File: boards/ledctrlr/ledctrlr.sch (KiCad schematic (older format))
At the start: 55 parts, among them IC1 ATMEGA168-P, IC2 SN75176B, J1 RJ45, J2 RJ45, SW1 SW_PUSH, U1 LM7805, X1 CRYSTAL

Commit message: rev 2.0 routed
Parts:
- LED0, LED2, LED3, LED4: DigikeyPart (none) -> ED2563-ND; Part (none) -> OSTTA040161
- LED1: Digikey (none) -> ED2563-ND; Part (none) -> OSTTA040161
- TLC1, TLC2, TLC3: footprint (none) -> DIP-28__300; DigikeyPart (none) -> 296-17732-5-ND; Part (none) -> TLC5940NT
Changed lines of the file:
@@
-EESchema Schematic File Version 2  date Mon 29 Oct 2012 07:47:27 PM EDT
+EESchema Schematic File Version 2  date Sat 03 Nov 2012 11:20:31 PM EDT
 LIBS:power
 LIBS:device
@@
 Sheet 1 1
 Title "5-RGB LED Controller Board"
-Date "29 oct 2012"
+Date "4 nov 2012"
 Rev "2.0"
 Comp "J. Colosimo"
@@
 F 1 "CONN_4" V 10300 2950 50  0000 C CNN
 F 2 "OSTTA040161" V 10400 2950 50  0001 C CNN
+F 4 "OSTTA040161" H 10250 2950 60  0001 C CNN "Part"
+F 5 "ED2563-ND" V 10250 2950 60  0001 C CNN "DigikeyPart"
 	1    10250 2950
 	1    0    0    -1
@@
 F 1 "CONN_4" V 10300 3450 50  0000 C CNN
 F 2 "OSTTA040161" V 10400 3450 50  0001 C CNN
+F 4 "OSTTA040161" H 10250 3450 60  0001 C CNN "Part"
+F 5 "ED2563-ND" V 10250 3450 60  0001 C CNN "Digikey"
 	1    10250 3450
 	1    0    0    -1
@@
 F 1 "CONN_4" V 10300 3950 50  0000 C CNN
 F 2 "OSTTA040161" V 10400 3950 50  0001 C CNN
+F 4 "OSTTA040161" H 10250 3950 60  0001 C CNN "Part"
+F 5 "ED2563-ND" V 10250 3950 60  0001 C CNN "DigikeyPart"
 	1    10250 3950
 	1    0    0    -1
@@
 F 1 "CONN_4" V 10300 4450 50  0000 C CNN
 F 2 "OSTTA040161" V 10400 4450 50  0001 C CNN
+F 4 "OSTTA040161" H 10250 4450 60  0001 C CNN "Part"
+F 5 "ED2563-ND" V 10250 4450 60  0001 C CNN "DigikeyPart"
 	1    10250 4450
 	1    0    0    -1
@@
 F 1 "CONN_4" V 10300 4950 50  0000 C CNN
 F 2 "OSTTA040161" V 10400 4950 50  0001 C CNN
+F 4 "OSTTA040161" H 10250 4950 60  0001 C CNN "Part"
+F 5 "ED2563-ND" V 10250 4950 60  0001 C CNN "DigikeyPart"
 	1    10250 4950
 	1    0    0    -1
@@
 F 0 "TLC1" H 7800 2300 60  0000 C CNN
 F 1 "TLC5940" H 7850 1750 60  0000 C CNN
+F 2 "DIP-28__300" H 7850 1850 60  0001 C CNN
+F 4 "TLC5940NT" H 7800 1550 60  0001 C CNN "Part"
+F 5 "296-17732-5-ND" H 7800 1550 60  0001 C CNN "DigikeyPart"
 	1    7800 1550
 	-1   0    0    -1
@@
 F 0 "TLC2" H 7800 4450 60  0000 C CNN
 F 1 "TLC5940" H 7850 3900 60  0000 C CNN
+F 2 "DIP-28__300" H 7850 4000 60  0001 C CNN
+F 4 "TLC5940NT" H 7800 3700 60  0001 C CNN "Part"
+F 5 "296-17732-5-ND" H 7800 3700 60  0001 C CNN "DigikeyPart"
 	1    7800 3700
 	-1   0    0    -1
@@
 F 0 "TLC3" H 7800 6600 60  0000 C CNN
 F 1 "TLC5940" H 7850 6050 60  0000 C CNN
+F 2 "DIP-28__300" H 7850 6150 60  0001 C CNN
+F 4 "TLC5940NT" H 7800 5850 60  0001 C CNN "Part"
+F 5 "296-17732-5-ND" H 7800 5850 60  0001 C CNN "DigikeyPart"
 	1    7800 5850
 	-1   0    0    -1

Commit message: clean up routing, switch GSCLK to PB0
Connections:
- net GSCLK: now also IC1.14 ((PCINT0/CLKO/ICP1)PB0); no longer IC1.5 ((PCINT19/OC2B/INT1)PD3)
- net XPB0 renamed XPD3
- net XPD3: now also IC1.5 ((PCINT19/OC2B/INT1)PD3); no longer IC1.14 ((PCINT0/CLKO/ICP1)PB0)
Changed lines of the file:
@@
-EESchema Schematic File Version 2  date Sat 03 Nov 2012 11:20:31 PM EDT
+EESchema Schematic File Version 2  date Mon 05 Nov 2012 06:34:16 PM EST
 LIBS:power
 LIBS:device
@@
 Sheet 1 1
 Title "5-RGB LED Controller Board"
-Date "4 nov 2012"
+Date "5 nov 2012"
 Rev "2.0"
 Comp "J. Colosimo"
@@
 F 5 "N/A" H 4700 4500 60  0001 C CNN "DigikeyPart"
 	1    4700 4500
-	1    0    0    -1
-$EndComp
-$Comp
-L CONN_1 PX2
-U 1 1 4DDC2882
-P 4700 2500
-F 0 "PX2" H 4750 2500 40  0000 L CNN
-F 1 "CONN_1" H 4700 2555 30  0001 C CNN
-F 2 "PAD" H 4790 2460 60  0001 C CNN
-F 4 "N/A" H 4700 2500 60  0001 C CNN "Part"
-F 5 "N/A" H 4700 2500 60  0001 C CNN "DigikeyPart"
-	1    4700 2500
 	1    0    0    -1
 $EndComp
@@
 Text Label 5300 2700 0    60   ~ 0
 BLANK
-Text Label 5350 4400 0    60   ~ 0
+Text Label 5300 2500 0    60   ~ 0
 GSCLK
 Text Label 4600 4600 0    60   ~ 0
@@
 Text Label 4700 2100 0    60   ~ 0
 XTAL2
-Text Label 4500 2500 0    60   ~ 0
-XPB0
 Text Label 4500 2900 0    60   ~ 0
 XPB4
@@
 	-1   0    0    1
 $EndComp
+$Comp
+L CONN_1 PX2
+U 1 1 50984858
+P 4700 4400
+F 0 "PX2" H 4750 4400 40  0000 L CNN
+F 1 "CONN_1" H 4700 4455 30  0001 C CNN
+F 2 "PAD" H 4790 4360 60  0001 C CNN
+F 4 "N/A" H 4700 4400 60  0001 C CNN "Part"
+F 5 "N/A" H 4700 4400 60  0001 C CNN "DigikeyPart"
+	1    4700 4400
+	1    0    0    -1
+$EndComp
+Text Label 4500 4400 0    60   ~ 0
+XPD3
 Wire Wire Line
 	1700 1550 1700 1850
@@
 Wire Wire Line
 	6400 2600 4500 2600
-Connection ~ 6650 4400
-Wire Wire Line
-	4500 4400 6650 4400
 Wire Wire Line
 	6150 950  7200 950
@@
 	4500 3850 4550 3850
 Wire Wire Line
-	4500 2500 4550 2500
-Wire Wire Line
 	2100 6300 2250 6300
 Connection ~ 2100 6300
@@
 Wire Wire Line
 	8000 5450 8000 5450
+Wire Wire Line
+	4500 4400 4550 4400
+Wire Wire Line
+	4500 2500 6650 2500
+Connection ~ 6650 2500
 $EndSCHEMATC

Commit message: clean up routing, return GSCLK to PD3, initial gerber export
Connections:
- net GSCLK: now also IC1.5 ((PCINT19/OC2B/INT1)PD3); no longer IC1.14 ((PCINT0/CLKO/ICP1)PB0)
- net XPD3 renamed XPB0
- net XPB0: now also IC1.14 ((PCINT0/CLKO/ICP1)PB0); no longer IC1.5 ((PCINT19/OC2B/INT1)PD3)
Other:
- moved on the sheet: PX2
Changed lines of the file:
@@
-EESchema Schematic File Version 2  date Mon 05 Nov 2012 06:34:16 PM EST
+EESchema Schematic File Version 2  date Wed 07 Nov 2012 06:37:59 AM EST
 LIBS:power
 LIBS:device
@@
 Sheet 1 1
 Title "5-RGB LED Controller Board"
-Date "5 nov 2012"
+Date "7 nov 2012"
 Rev "2.0"
 Comp "J. Colosimo"
@@
 Text Label 5300 2700 0    60   ~ 0
 BLANK
-Text Label 5300 2500 0    60   ~ 0
+Text Label 5300 4400 0    60   ~ 0
 GSCLK
 Text Label 4600 4600 0    60   ~ 0
@@
 L CONN_1 PX2
 U 1 1 50984858
-P 4700 4400
-F 0 "PX2" H 4750 4400 40  0000 L CNN
-F 1 "CONN_1" H 4700 4455 30  0001 C CNN
-F 2 "PAD" H 4790 4360 60  0001 C CNN
-F 4 "N/A" H 4700 4400 60  0001 C CNN "Part"
-F 5 "N/A" H 4700 4400 60  0001 C CNN "DigikeyPart"
-	1    4700 4400
-	1    0    0    -1
-$EndComp
-Text Label 4500 4400 0    60   ~ 0
-XPD3
+P 4700 2500
+F 0 "PX2" H 4750 2500 40  0000 L CNN
+F 1 "CONN_1" H 4700 2555 30  0001 C CNN
+F 2 "PAD" H 4790 2460 60  0001 C CNN
+F 4 "N/A" H 4700 2500 60  0001 C CNN "Part"
+F 5 "N/A" H 4700 2500 60  0001 C CNN "DigikeyPart"
+	1    4700 2500
+	1    0    0    -1
+$EndComp
+Text Label 4500 2500 0    60   ~ 0
+XPB0
 Wire Wire Line
 	1700 1550 1700 1850
@@
 	8000 5450 8000 5450
 Wire Wire Line
-	4500 4400 4550 4400
-Wire Wire Line
-	4500 2500 6650 2500
-Connection ~ 6650 2500
+	4500 4400 6650 4400
+Connection ~ 6650 4400
+Wire Wire Line
+	4500 2500 4550 2500
 $EndSCHEMATC

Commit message: clean up ground routing, get rid of npth
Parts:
- LED0, LED1, LED2, LED3, LED4: footprint OSTTA040161 -> OSTTA040161p
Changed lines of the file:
@@
-EESchema Schematic File Version 2  date Wed 07 Nov 2012 06:37:59 AM EST
+EESchema Schematic File Version 2  date Wed 14 Nov 2012 04:07:55 PM EST
 LIBS:power
 LIBS:device
@@
 F 0 "LED0" V 10200 2950 50  0000 C CNN
 F 1 "CONN_4" V 10300 2950 50  0000 C CNN
-F 2 "OSTTA040161" V 10400 2950 50  0001 C CNN
+F 2 "OSTTA040161p" V 10400 2950 50  0001 C CNN
 F 4 "OSTTA040161" H 10250 2950 60  0001 C CNN "Part"
 F 5 "ED2563-ND" V 10250 2950 60  0001 C CNN "DigikeyPart"
@@
 F 0 "LED1" V 10200 3450 50  0000 C CNN
 F 1 "CONN_4" V 10300 3450 50  0000 C CNN
-F 2 "OSTTA040161" V 10400 3450 50  0001 C CNN
+F 2 "OSTTA040161p" V 10400 3450 50  0001 C CNN
 F 4 "OSTTA040161" H 10250 3450 60  0001 C CNN "Part"
 F 5 "ED2563-ND" V 10250 3450 60  0001 C CNN "Digikey"
@@
 F 0 "LED2" V 10200 3950 50  0000 C CNN
 F 1 "CONN_4" V 10300 3950 50  0000 C CNN
-F 2 "OSTTA040161" V 10400 3950 50  0001 C CNN
+F 2 "OSTTA040161p" V 10400 3950 50  0001 C CNN
 F 4 "OSTTA040161" H 10250 3950 60  0001 C CNN "Part"
 F 5 "ED2563-ND" V 10250 3950 60  0001 C CNN "DigikeyPart"
@@
 F 0 "LED3" V 10200 4450 50  0000 C CNN
 F 1 "CONN_4" V 10300 4450 50  0000 C CNN
-F 2 "OSTTA040161" V 10400 4450 50  0001 C CNN
+F 2 "OSTTA040161p" V 10400 4450 50  0001 C CNN
 F 4 "OSTTA040161" H 10250 4450 60  0001 C CNN "Part"
 F 5 "ED2563-ND" V 10250 4450 60  0001 C CNN "DigikeyPart"
@@
 F 0 "LED4" V 10200 4950 50  0000 C CNN
 F 1 "CONN_4" V 10300 4950 50  0000 C CNN
-F 2 "OSTTA040161" V 10400 4950 50  0001 C CNN
+F 2 "OSTTA040161p" V 10400 4950 50  0001 C CNN
 F 4 "OSTTA040161" H 10250 4950 60  0001 C CNN "Part"
 F 5 "ED2563-ND" V 10250 4950 60  0001 C CNN "DigikeyPart"

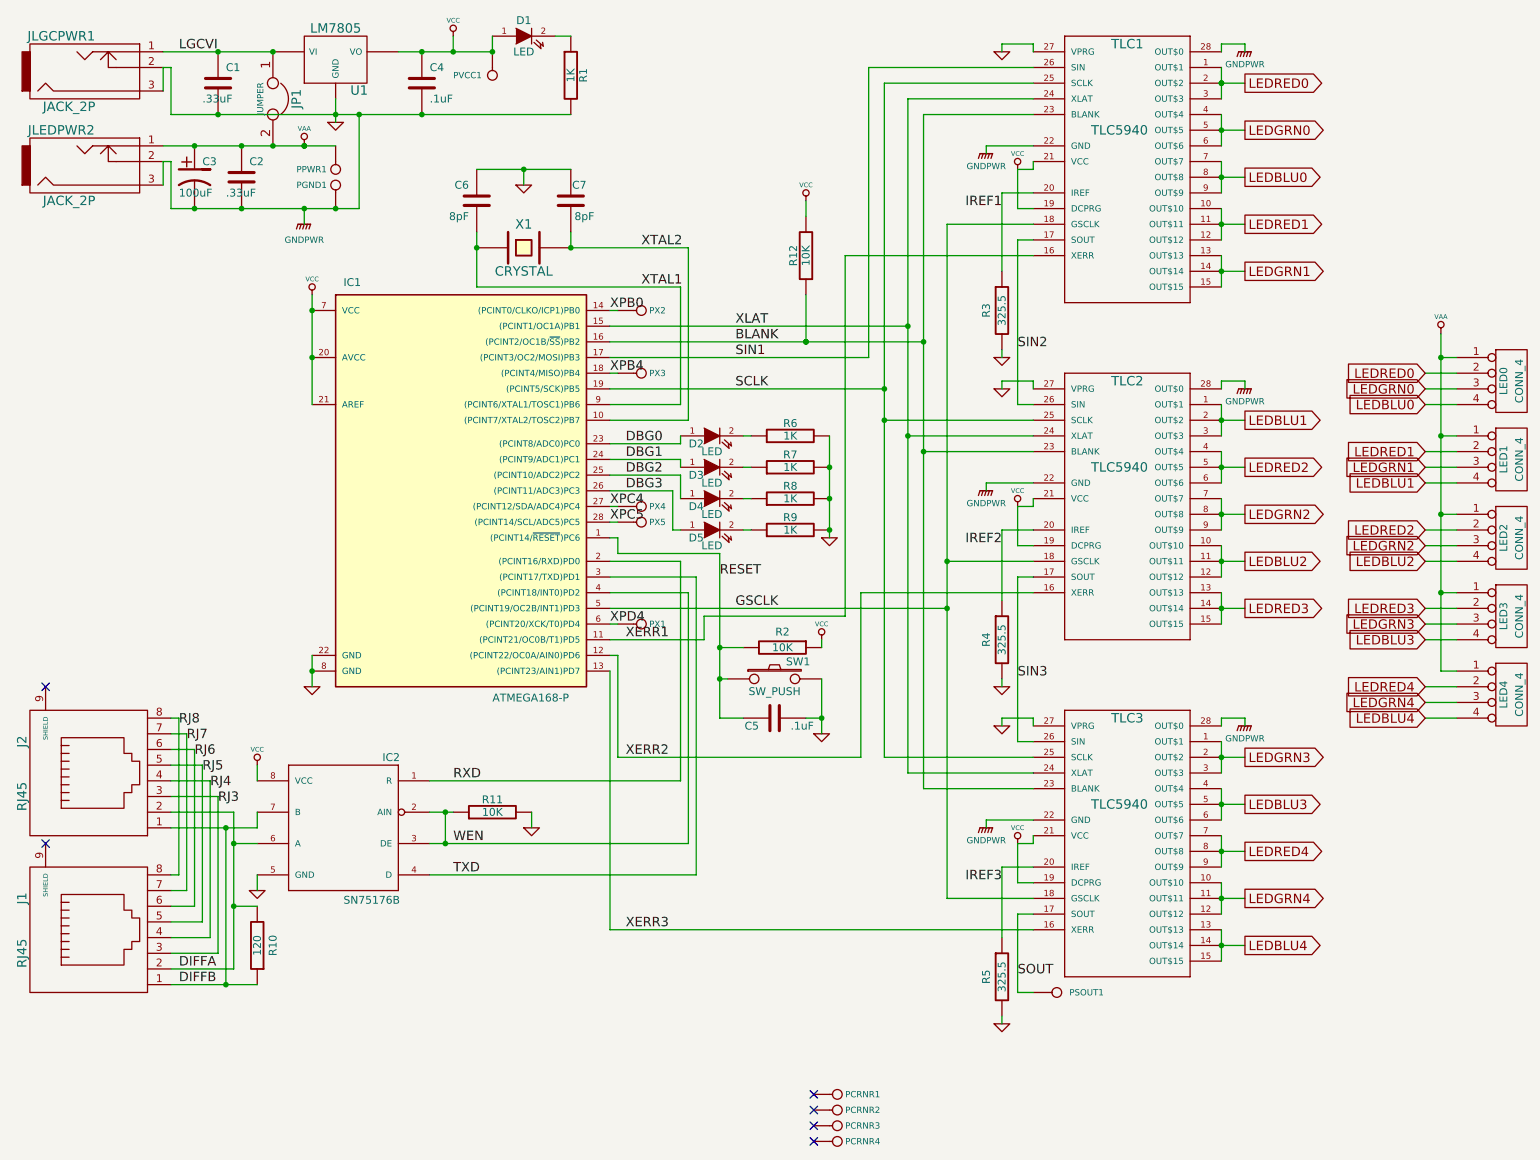
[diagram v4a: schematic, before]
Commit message: add schematics and footprints for green and black NRF24L01+ modules
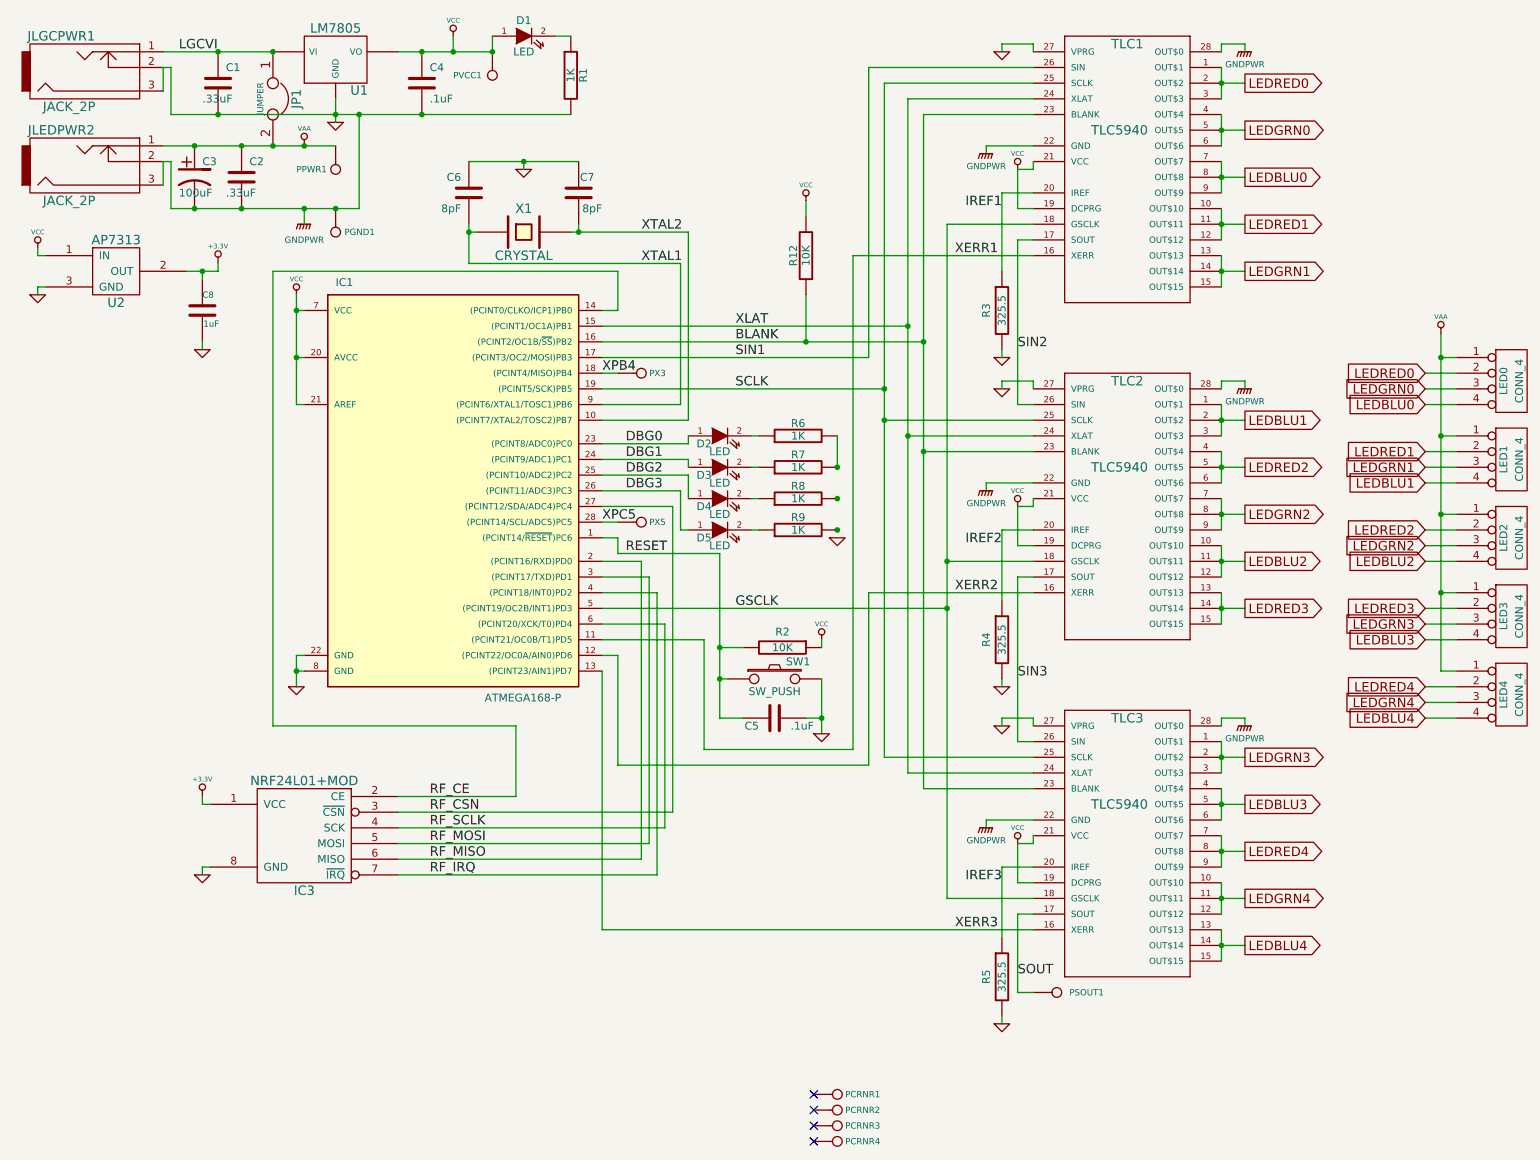
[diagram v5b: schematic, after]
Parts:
- removed IC2: SN75176B, SOIC8, symbol SN75176B
- removed J1, J2: RJ45, RJ45_8, symbol RJ45
- removed PX1, PX2, PX4: CONN_1, PAD, symbol CONN_1
- removed R10: 120, SM0805, symbol R
- removed R11: 10K, SM0805, symbol R
- added C8: 1uF, SM0805, symbol C
- added IC3: NRF24L01+MOD, NRF24LO1+MOD_GRN, symbol NRF24L01+MOD
- added U2: AP7313, SOT23, symbol AP7313
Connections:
- net GND: now also C8.2, IC3.8 (GND), U2.3 (GND); no longer R6.2, R7.2, R8.2, R9.2
- net VCC: now also U2.1 (IN)
- net RXD renamed RF_MISO
- net RF_MISO: now also IC3.6 (MISO)
- net TXD renamed RF_MOSI
- net RF_MOSI: now also IC3.5 (MOSI)
- net WEN renamed RF_IRQ
- net RF_IRQ: now also IC3.7 (~IRQ)
- net XPB0 renamed RF_CE
- net RF_CE: now also IC3.2 (CE)
- net XPC4 renamed RF_CSN
- net RF_CSN: now also IC3.3 (~CSN)
- net XPD4 renamed RF_SCLK
- net RF_SCLK: now also IC3.4 (SCK)
- new net: R6.2, R7.2
- new net +3.3V: C8.1, IC3.1 (VCC), U2.2 (OUT)
- no-connect marks 6 -> 4
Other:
- moved on the sheet: C6, C7, D2, D3, D4, D5, IC1, PGND1, R6, R7, R8, R9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

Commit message: transmit appears to be working
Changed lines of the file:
@@
 	6150 4300 7200 4300
 Wire Wire Line
-	1700 1250 4250 1250
+	1700 1250 2000 1250
+Wire Wire Line
+	2000 1250 2750 1250
+Wire Wire Line
+	2750 1250 2900 1250
+Wire Wire Line
+	2900 1250 3300 1250
+Wire Wire Line
+	3300 1250 4250 1250
 Connection ~ 5950 3700
 Connection ~ 5200 4850
@@
 	6650 6250 7200 6250
 Wire Wire Line
-	6650 1950 6650 6250
+	6650 1950 6650 4100
+Wire Wire Line
+	6650 4100 6650 4400
+Wire Wire Line
+	6650 4400 6650 6250
 Wire Wire Line
 	7100 1850 7100 1600
@@
 Connection ~ 8400 4400
 Wire Wire Line
-	8400 4300 8400 4500
+	8400 4300 8400 4400
+Wire Wire Line
+	8400 4400 8400 4500
 Connection ~ 8400 4100
 Wire Wire Line
-	8400 4000 8400 4200
+	8400 4000 8400 4100
+Wire Wire Line
+	8400 4100 8400 4200
 Connection ~ 8400 3800
 Wire Wire Line
-	8400 3700 8400 3900
+	8400 3700 8400 3800
+Wire Wire Line
+	8400 3800 8400 3900
 Connection ~ 8400 3500
 Wire Wire Line
-	8400 3400 8400 3600
+	8400 3400 8400 3500
+Wire Wire Line
+	8400 3500 8400 3600
 Connection ~ 8400 3200
 Wire Wire Line
-	8400 3100 8400 3300
+	8400 3100 8400 3200
+Wire Wire Line
+	8400 3200 8400 3300
 Wire Wire Line
 	7200 3900 7000 3900
@@
 	7000 6050 7200 6050
 Wire Wire Line
-	8400 5250 8400 5450
+	8400 5250 8400 5350
+Wire Wire Line
+	8400 5350 8400 5450
 Connection ~ 8400 5350
 Wire Wire Line
-	8400 5550 8400 5750
+	8400 5550 8400 5650
+Wire Wire Line
+	8400 5650 8400 5750
 Connection ~ 8400 5650
 Wire Wire Line
-	8400 5850 8400 6050
+	8400 5850 8400 5950
+Wire Wire Line
+	8400 5950 8400 6050
 Connection ~ 8400 5950
 Wire Wire Line
-	8400 6150 8400 6350
+	8400 6150 8400 6250
+Wire Wire Line
+	8400 6250 8400 6350
 Connection ~ 8400 6250
 Wire Wire Line
-	8400 6450 8400 6650
+	8400 6450 8400 6550
+Wire Wire Line
+	8400 6550 8400 6650
 Connection ~ 8400 6550
 Wire Wire Line
@@
 	6500 5550 7200 5550
 Wire Wire Line
-	6500 1250 6500 5550
+	6500 1250 6500 2700
+Wire Wire Line
+	6500 2700 6500 3400
+Wire Wire Line
+	6500 3400 6500 5550
 Wire Wire Line
 	6400 5450 7200 5450
@@
 	7200 1150 6400 1150
 Wire Wire Line
-	6250 1050 6250 5350
+	6250 1050 6250 3000
+Wire Wire Line
+	6250 3000 6250 3200
+Wire Wire Line
+	6250 3200 6250 5350
 Wire Wire Line
 	6250 5350 7200 5350
@@
 	4450 4300 4800 4300
 Wire Wire Line
-	4450 2700 6500 2700
+	4450 2700 5750 2700
+Wire Wire Line
+	5750 2700 6500 2700
 Connection ~ 6500 2700
 Wire Wire Line
@@
 	6250 3000 4450 3000
 Wire Wire Line
-	6400 1150 6400 5450
-Wire Wire Line
-	2750 1150 2750 1300
+	6400 1150 6400 2600
+Wire Wire Line
+	6400 2600 6400 3300
+Wire Wire Line
+	6400 3300 6400 5450
+Wire Wire Line
+	2750 1150 2750 1250
+Wire Wire Line
+	2750 1250 2750 1300
 Connection ~ 2000 850
 Connection ~ 2750 1250
@@
 Connection ~ 3500 850
 Wire Wire Line
-	3150 850  3750 850
+	3150 850  3300 850
+Wire Wire Line
+	3300 850  3500 850
+Wire Wire Line
+	3500 850  3750 850
 Wire Wire Line
 	5200 5100 5350 5100
@@
 	4550 4050 5200 4050
 Wire Wire Line
-	5200 4050 5200 5100
+	5200 4050 5200 4650
+Wire Wire Line
+	5200 4650 5200 4850
+Wire Wire Line
+	5200 4850 5200 5100
 Connection ~ 5200 4650
 Connection ~ 5950 3500
@@
 	5100 4600 4450 4600
 Wire Wire Line
-	1700 1850 2900 1850
+	1700 1850 1850 1850
+Wire Wire Line
+	1850 1850 2150 1850
+Wire Wire Line
+	2150 1850 2550 1850
+Wire Wire Line
+	2550 1850 2750 1850
+Wire Wire Line
+	2750 1850 2900 1850
 Connection ~ 2550 1850
 Wire Wire Line
@@
 	4800 4300 4800 6100
 Wire Wire Line
-	1650 850  2350 850
-Wire Wire Line
-	1650 1450 2750 1450
-Wire Wire Line
-	9800 2650 9800 4800
+	1650 850  2000 850
+Wire Wire Line
+	2000 850  2350 850
+Wire Wire Line
+	1650 1450 1850 1450
+Wire Wire Line
+	1850 1450 2150 1450
+Wire Wire Line
+	2150 1450 2350 1450
+Wire Wire Line
+	2350 1450 2550 1450
+Wire Wire Line
+	2550 1450 2750 1450
+Wire Wire Line
+	9800 2650 9800 2800
+Wire Wire Line
+	9800 2800 9800 3300
+Wire Wire Line
+	9800 3300 9800 3800
+Wire Wire Line
+	9800 3800 9800 4300
+Wire Wire Line
+	9800 4300 9800 4800
 Wire Wire Line
 	9800 2800 9900 2800
@@
 	1650 1550 1650 1700
 Wire Wire Line
-	5850 4850 5850 5200
+	5850 4850 5850 5100
+Wire Wire Line
+	5850 5100 5850 5200
 Wire Wire Line
 	5750 5100 5850 5100
@@
 	8400 800  8400 850
 Wire Wire Line
-	8400 950  8400 1150
+	8400 950  8400 1050
+Wire Wire Line
+	8400 1050 8400 1150
 Connection ~ 8400 1050
 Wire Wire Line
-	8400 1250 8400 1450
+	8400 1250 8400 1350
+Wire Wire Line
+	8400 1350 8400 1450
 Connection ~ 8400 1350
 Wire Wire Line
-	8400 1550 8400 1750
+	8400 1550 8400 1650
+Wire Wire Line
+	8400 1650 8400 1750
 Connection ~ 8400 1650
 Wire Wire Line
-	8400 1850 8400 2050
+	8400 1850 8400 1950
+Wire Wire Line
+	8400 1950 8400 2050
 Connection ~ 8400 1950
 Wire Wire Line
-	8400 2150 8400 2350
+	8400 2150 8400 2250
+Wire Wire Line
+	8400 2250 8400 2350
 Connection ~ 8400 2250
 Wire Wire Line
@@
 	850  2350 850  2400
 Wire Wire Line
-	1800 2250 2000 2250
+	1800 2250 1900 2250
+Wire Wire Line
+	1900 2250 2000 2250
 Wire Wire Line
 	2000 2250 2000 2200
@@
 	3600 2200 4950 2200
 Wire Wire Line
-	3600 1950 3600 2200
+	3600 1950 3600 2000
+Wire Wire Line
+	3600 2000 3600 2200
 Wire Wire Line
 	3650 2000 3600 2000
 Connection ~ 3600 2000
 Wire Wire Line
-	4250 2000 5000 2000
+	4250 2000 4300 2000
+Wire Wire Line
+	4300 2000 5000 2000
 Wire Wire Line
 	4300 1950 4300 2000
 Connection ~ 4300 2000
 Wire Wire Line
-	3600 1550 4300 1550
+	3600 1550 3950 1550
+Wire Wire Line
+	3950 1550 4300 1550
 Wire Wire Line
 	3950 1600 3950 1550
@@
 	4450 6450 4450 4800
 Wire Wire Line
-	2500 2400 2500 3100
+	2500 2400 2500 2500
+Wire Wire Line
+	2500 2500 2500 2800
+Wire Wire Line
+	2500 2800 2500 3100
 Wire Wire Line
 	2500 3100 2550 3100
@@
 	2550 4700 2500 4700
 Wire Wire Line
-	2500 4700 2500 4900
+	2500 4700 2500 4800
+Wire Wire Line
+	2500 4800 2500 4900
 Wire Wire Line
 	2550 4800 2500 4800
